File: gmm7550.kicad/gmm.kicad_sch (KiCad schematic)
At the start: 8 parts

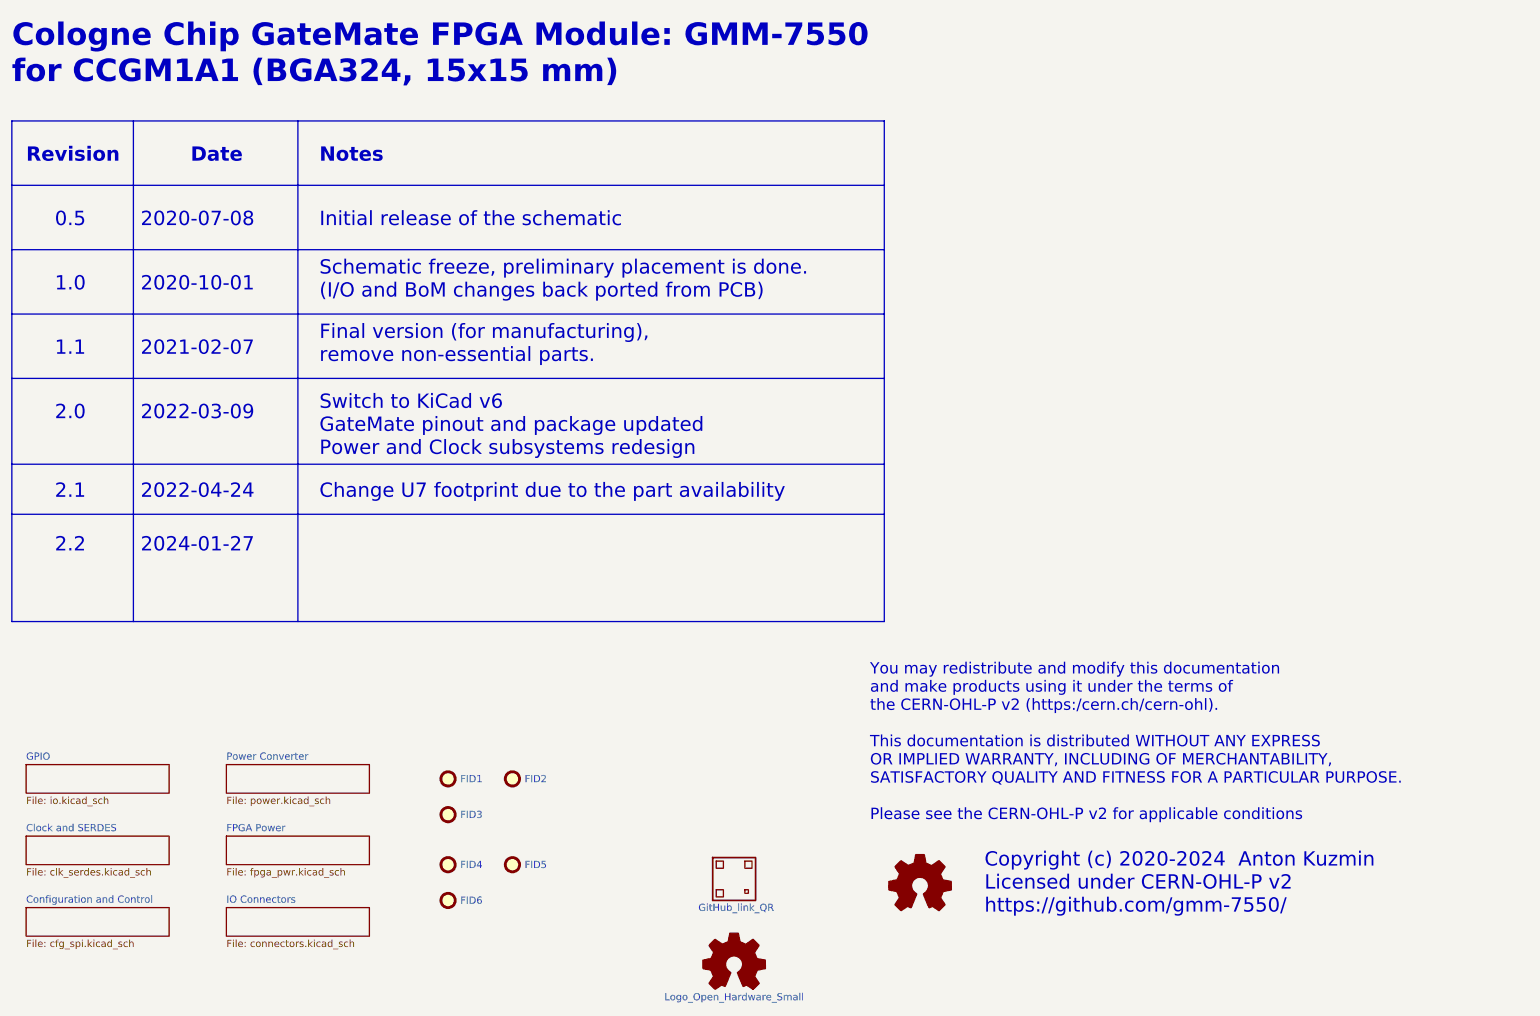
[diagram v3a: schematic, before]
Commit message: Minor updates based on the test results
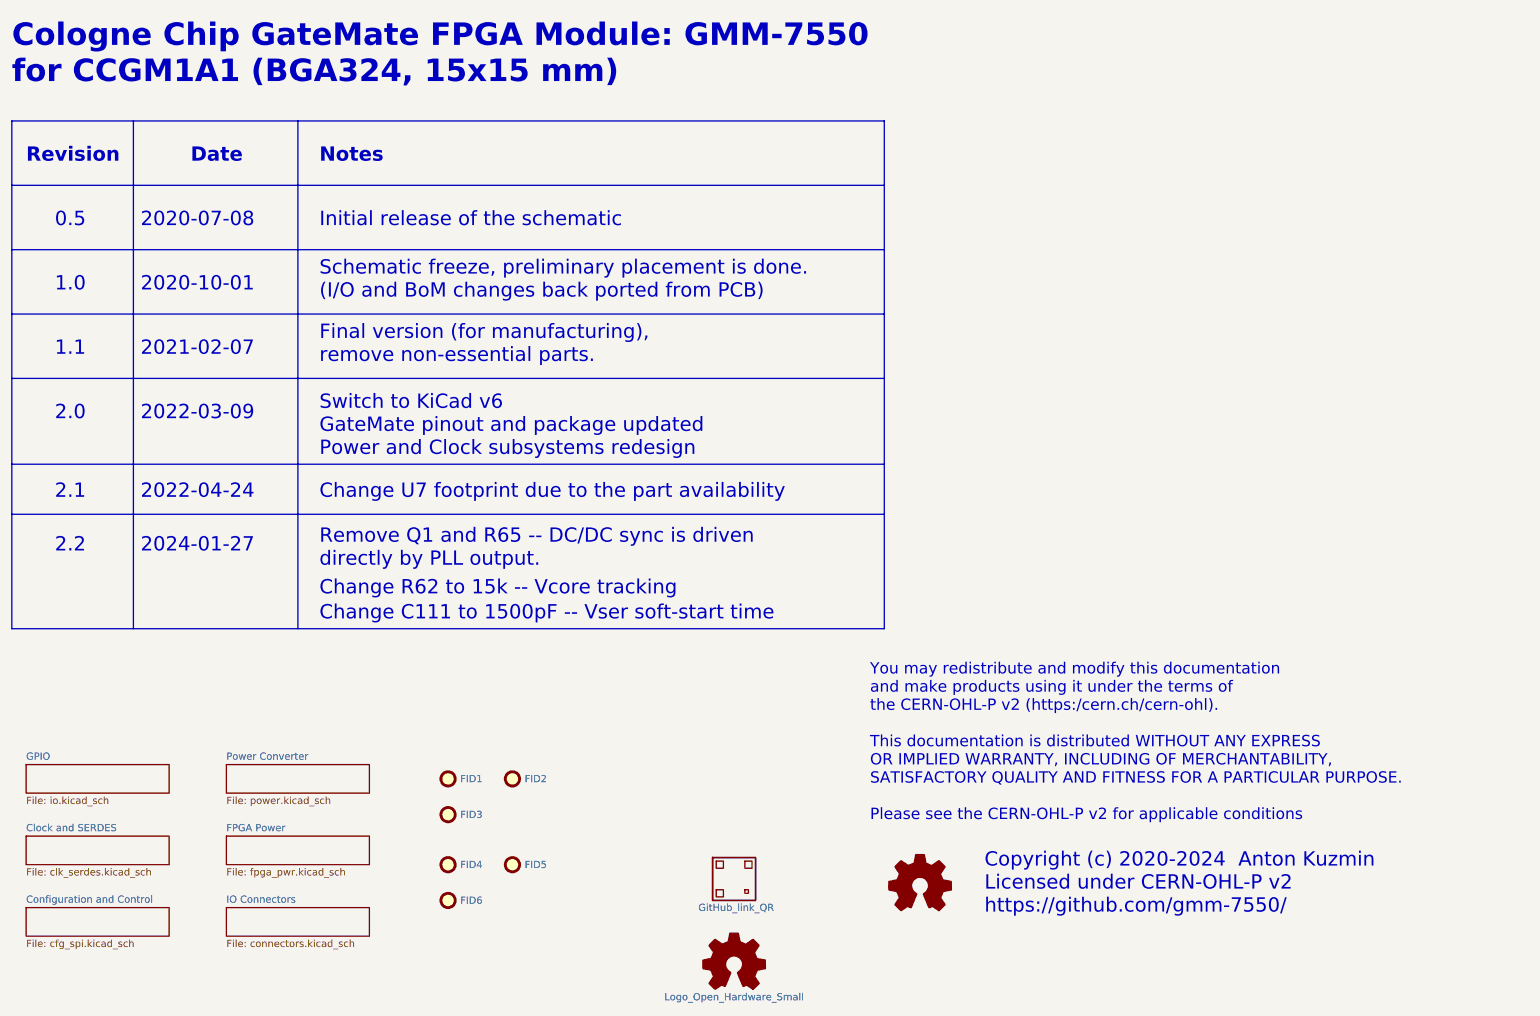
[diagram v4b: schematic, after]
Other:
- note added: "Change C111 to 1500pF -- Vser soft-start time"
- note added: "Change R62 to 15k -- Vcore tracking"
- note added: "Remove Q1 and R65 -- DC/DC sync is driven directly by PLL output."
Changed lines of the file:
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@@
     (stroke (width 0.2032) (type solid))
   )
-  (polyline (pts (xy 180.34 38.1) (xy 180.34 127))
+  (polyline (pts (xy 180.34 38.1) (xy 180.34 128.27))
     (stroke (width 0.2032) (type solid))
   )
-  (polyline (pts (xy 46.99 38.1) (xy 46.99 127))
+  (polyline (pts (xy 46.99 38.1) (xy 46.99 128.27))
     (stroke (width 0.2032) (type solid))
   )
@@
     (stroke (width 0.2032) (type solid))
   )
-  (polyline (pts (xy 76.2 38.1) (xy 76.2 127))
+  (polyline (pts (xy 76.2 38.1) (xy 76.2 128.27))
     (stroke (width 0.2032) (type solid))
   )
@@
     (stroke (width 0.2032) (type solid))
   )
-  (polyline (pts (xy 25.4 38.1) (xy 25.4 127))
+  (polyline (pts (xy 25.4 38.1) (xy 25.4 128.27))
     (stroke (width 0.2032) (type solid))
   )
-  (polyline (pts (xy 25.4 127) (xy 180.34 127))
+  (polyline (pts (xy 25.4 128.27) (xy 180.34 128.27))
     (stroke (width 0.2032) (type solid))
   )
@@
   )
   (text "0.5" (at 33.02 57.15 0)
+    (effects (font (size 2.54 2.54)) (justify left bottom))
+  )
+  (text "Change C111 to 1500pF -- Vser soft-start time" (at 80.01 127 0)
     (effects (font (size 2.54 2.54)) (justify left bottom))
   )
@@
   )
   (text "2021-02-07" (at 48.26 80.01 0)
+    (effects (font (size 2.54 2.54)) (justify left bottom))
+  )
+  (text "Change R62 to 15k -- Vcore tracking" (at 80.01 122.555 0)
     (effects (font (size 2.54 2.54)) (justify left bottom))
   )
@@
     (effects (font (size 2.54 2.54)) (justify left bottom))
   )
+  (text "Remove Q1 and R65 -- DC/DC sync is driven\ndirectly by PLL output."
+    (at 80.01 117.475 0)
+    (effects (font (size 2.54 2.54)) (justify left bottom))
+  )

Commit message: Update QR-code with a link to the project web site
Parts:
- QR1: footprint gmm:GitHub_link_QR -> gmm:gmm7550_dev_link_QR
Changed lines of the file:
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@@
       (effects (font (size 1.27 1.27)) (justify left))
     )
-    (property "Footprint" "gmm:GitHub_link_QR" (at 153.67 172.72 0)
+    (property "Footprint" "gmm:gmm7550_dev_link_QR" (at 153.67 172.72 0)
       (effects (font (size 1.27 1.27)) hide)
     )
